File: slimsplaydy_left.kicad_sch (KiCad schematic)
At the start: 21 parts

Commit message: Add production files.
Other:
- title: (none) -> slimsplaydy_left
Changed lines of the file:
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@@
 	(generator_version "9.0")
 	(paper "A4")
+	(title_block
+		(title "slimsplaydy_left")
+		(date "2025-06-18")
+		(rev "1.0")
+	)
 	(text "The order of these switch refs is \ncounterintuitive but important: \nthey match the order in which \nergogen creates them."
 		(exclude_from_sim no)

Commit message: Cleanup ergogen and other from ezmate 1.0mm -> 1.2mm swap
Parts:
- CONN1: footprint Molex_Pico_EZMate_Plus_1x02 -> Connector_Molex:Molex_Pico-EZmate_78171-0002_1x02-1MP_P1.20mm_Vertical
- MCU1: symbol huntercooh:nice_nano_raw21 -> huntercook:nice_nano_raw21
- S1, S10, S11, S12, S13, S14, S15, S16, S17, S2, S3, S4, S5, S6, S7, S8, S9: symbol huntercooh:PG1316S -> huntercook:PG1316S
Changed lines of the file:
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@@
 			)
 		)
-		(property "Footprint" "Molex_Pico_EZMate_Plus_1x02"
+		(property "Footprint" "Connector_Molex:Molex_Pico-EZmate_78171-0002_1x02-1MP_P1.20mm_Vertical"
 			(at 245.11 144.78 0)
 			(effects
@@
 	)
 	(symbol
-		(lib_id "huntercooh:PG1316S")
+		(lib_id "huntercook:PG1316S")
 		(at 55.88 71.12 0)
 		(unit 1)
@@
 	)
 	(symbol
-		(lib_id "huntercooh:PG1316S")
+		(lib_id "huntercook:PG1316S")
 		(at 38.1 97.79 0)
 		(unit 1)
@@
 	)
 	(symbol
-		(lib_id "huntercooh:PG1316S")
+		(lib_id "huntercook:PG1316S")
 		(at 72.39 97.79 0)
 		(unit 1)
@@
 	)
 	(symbol
-		(lib_id "huntercooh:nice_nano_raw21")
+		(lib_id "huntercook:nice_nano_raw21")
 		(at 204.47 71.12 0)
 		(mirror y)
@@
 	)
 	(symbol
-		(lib_id "huntercooh:PG1316S")
+		(lib_id "huntercook:PG1316S")
 		(at 88.9 44.45 0)
 		(unit 1)
@@
 	)
 	(symbol
-		(lib_id "huntercooh:PG1316S")
+		(lib_id "huntercook:PG1316S")
 		(at 72.39 71.12 0)
 		(unit 1)
@@
 	)
 	(symbol
-		(lib_id "huntercooh:PG1316S")
+		(lib_id "huntercook:PG1316S")
 		(at 38.1 44.45 0)
 		(unit 1)
@@
 	)
 	(symbol
-		(lib_id "huntercooh:PG1316S")
+		(lib_id "huntercook:PG1316S")
 		(at 105.41 125.73 0)
 		(unit 1)
@@
 	)
 	(symbol
-		(lib_id "huntercooh:PG1316S")
+		(lib_id "huntercook:PG1316S")
 		(at 88.9 125.73 0)
 		(unit 1)
@@
 	)
 	(symbol
-		(lib_id "huntercooh:PG1316S")
+		(lib_id "huntercook:PG1316S")
 		(at 55.88 97.79 0)
 		(unit 1)
@@
 	)
 	(symbol
-		(lib_id "huntercooh:PG1316S")
+		(lib_id "huntercook:PG1316S")
 		(at 88.9 97.79 0)
 		(unit 1)
@@
 	)
 	(symbol
-		(lib_id "huntercooh:PG1316S")
+		(lib_id "huntercook:PG1316S")
 		(at 88.9 71.12 0)
 		(unit 1)
@@
 	)
 	(symbol
-		(lib_id "huntercooh:PG1316S")
+		(lib_id "huntercook:PG1316S")
 		(at 38.1 71.12 0)
 		(unit 1)
@@
 	)
 	(symbol
-		(lib_id "huntercooh:PG1316S")
+		(lib_id "huntercook:PG1316S")
 		(at 105.41 97.79 0)
 		(unit 1)
@@
 	)
 	(symbol
-		(lib_id "huntercooh:PG1316S")
+		(lib_id "huntercook:PG1316S")
 		(at 72.39 44.45 0)
 		(unit 1)
@@
 	)
 	(symbol
-		(lib_id "huntercooh:PG1316S")
+		(lib_id "huntercook:PG1316S")
 		(at 55.88 44.45 0)
 		(unit 1)
@@
 	)
 	(symbol
-		(lib_id "huntercooh:PG1316S")
+		(lib_id "huntercook:PG1316S")
 		(at 105.41 44.45 0)
 		(unit 1)
@@
 	)
 	(symbol
-		(lib_id "huntercooh:PG1316S")
+		(lib_id "huntercook:PG1316S")
 		(at 105.41 71.12 0)
 		(unit 1)

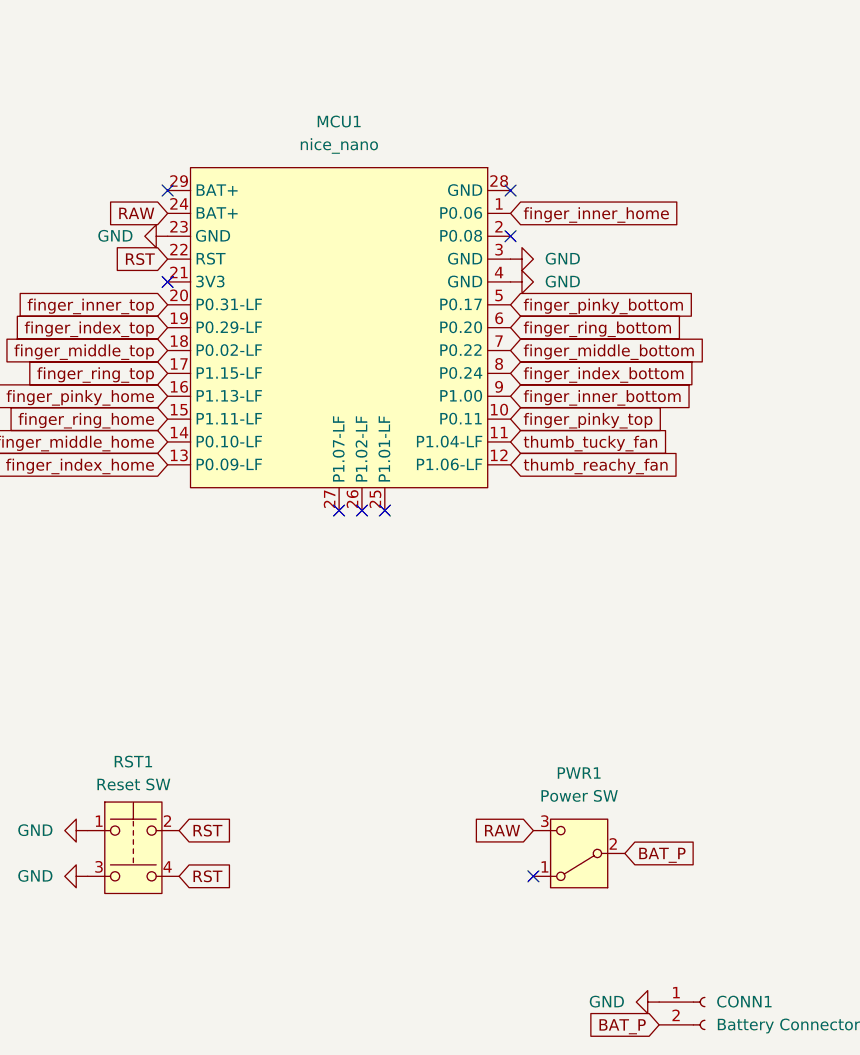
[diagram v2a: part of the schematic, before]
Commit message: Added LCSC fields to all parts.
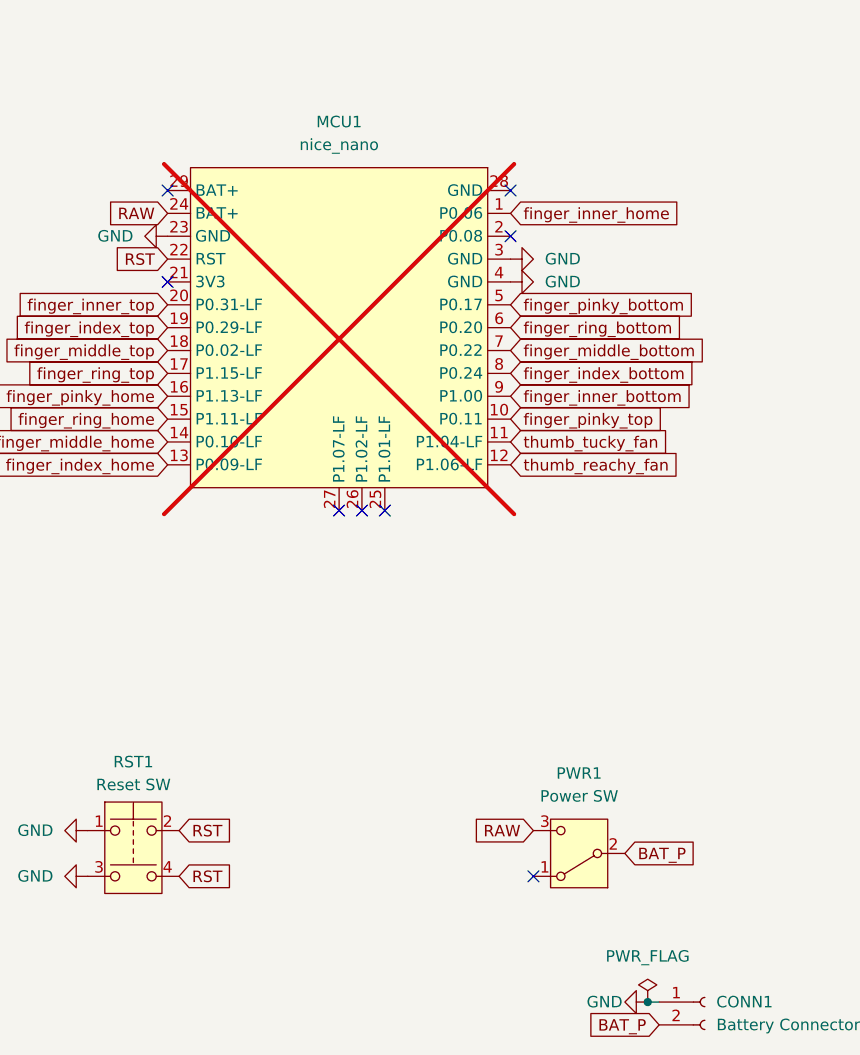
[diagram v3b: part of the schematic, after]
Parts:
- CONN1: LCSC (none) -> C505023
- MCU1: footprint ceoloide:mcu_nice_nano -> PCM_marbastlib-xp-promicroish:nice_nano_AH_USBup; LCSC (none) -> DNP; now not fitted
- PWR1: LCSC (none) -> C2911519
- RST1: LCSC (none) -> C79174
- S1, S10, S11, S12, S13, S14, S15, S16, S17, S2, S3, S4, S5, S6, S7, S8, S9: LCSC (none) -> C9900170245

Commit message: Fix nice_nano symbol so pins are power driven.
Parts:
- MCU1: footprint PCM_marbastlib-xp-promicroish:nice_nano_AH_USBup -> ceoloide:mcu_nice_nano
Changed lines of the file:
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@@
 			)
 		)
-		(property "Footprint" "PCM_marbastlib-xp-promicroish:nice_nano_AH_USBup"
+		(property "Footprint" "ceoloide:mcu_nice_nano"
 			(at 204.47 101.6 0)
 			(effects
